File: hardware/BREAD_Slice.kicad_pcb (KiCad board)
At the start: 2 copper layers, 70 x 100 mm, 16 parts, among them J1 I2C_01x04, J2 Conn_01x10_Female

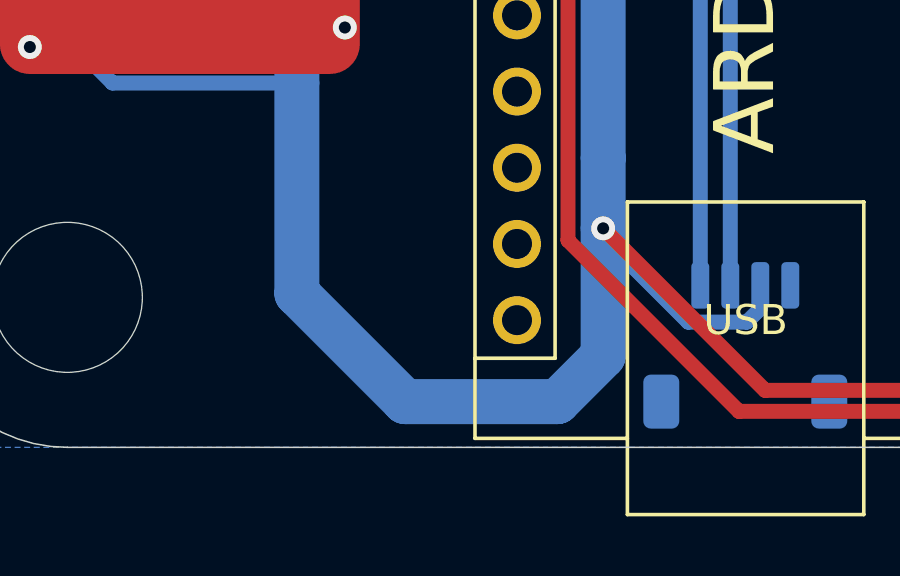
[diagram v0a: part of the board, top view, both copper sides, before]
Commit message: changed i2c connection to jst to simplify, fixed ground disconn around jst
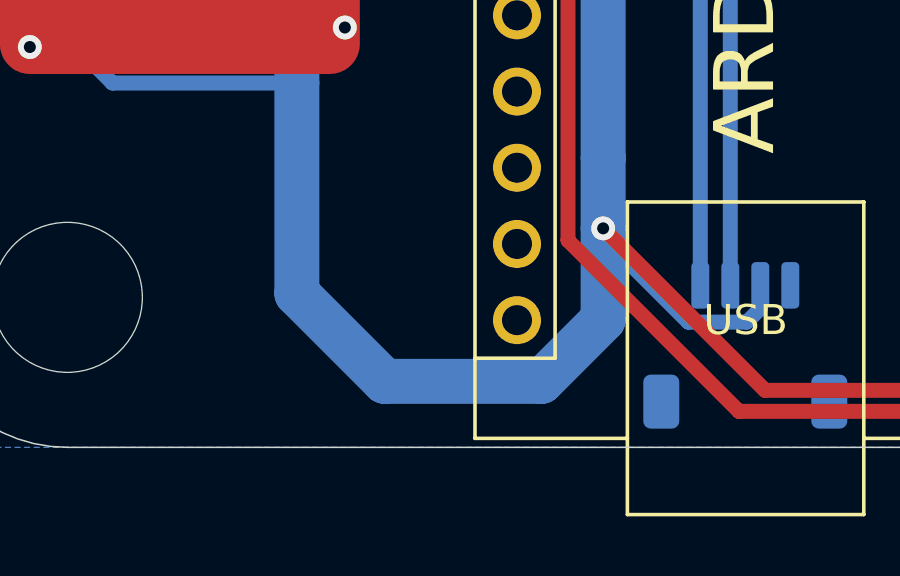
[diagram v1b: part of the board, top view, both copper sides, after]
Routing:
- net +5V: track 112.5 -> 111.2 mm
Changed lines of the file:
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@@
 	)
 	(segment
-		(start 138.856 138.276)
-		(end 143.936 138.276)
+		(start 138.18 137.6)
+		(end 143.4 137.6)
+		(width 1.5)
+		(layer "B.Cu")
+		(net 5)
+	)
+	(segment
+		(start 145.46 135.54)
+		(end 145.46 132.5)
+		(width 1.5)
+		(layer "B.Cu")
+		(net 5)
+	)
+	(segment
+		(start 135.25 134.67)
+		(end 138.18 137.6)
 		(width 1.5)
 		(layer "B.Cu")
@@
 	)
 	(segment
-		(start 143.936 138.276)
-		(end 145.46 136.752)
+		(start 143.4 137.6)
+		(end 145.46 135.54)
 		(width 1.5)
 		(layer "B.Cu")
@@
 	)
 	(segment
-		(start 145.46 132.5)
-		(end 145.46 130.148)
+		(start 135.25 127.655)
+		(end 135.25 134.67)
 		(width 1.5)
 		(layer "B.Cu")
@@
 	)
 	(segment
-		(start 135.25 127.655)
-		(end 135.25 134.67)
+		(start 145.46 132.5)
+		(end 145.46 130.148)
 		(width 1.5)
 		(layer "B.Cu")
@@
 	)
 	(segment
-		(start 145.46 136.752)
-		(end 145.46 132.5)
-		(width 1.5)
-		(layer "B.Cu")
-		(net 5)
-	)
-	(segment
 		(start 158.008 107.8)
 		(end 157.828 107.62)
@@
 		(width 1.5)
 		(layer "B.Cu")
-		(net 5)
-	)
-	(segment
-		(start 135.25 134.67)
-		(end 138.856 138.276)
-		(width 1.5)
-		(layer "B.Cu")
